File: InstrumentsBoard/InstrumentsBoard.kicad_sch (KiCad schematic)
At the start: 23 parts, among them J1 RJ45_LED_Shielded, Q1 BSS138, U1 Teensy4.1_DEV-16771, U2 OKI

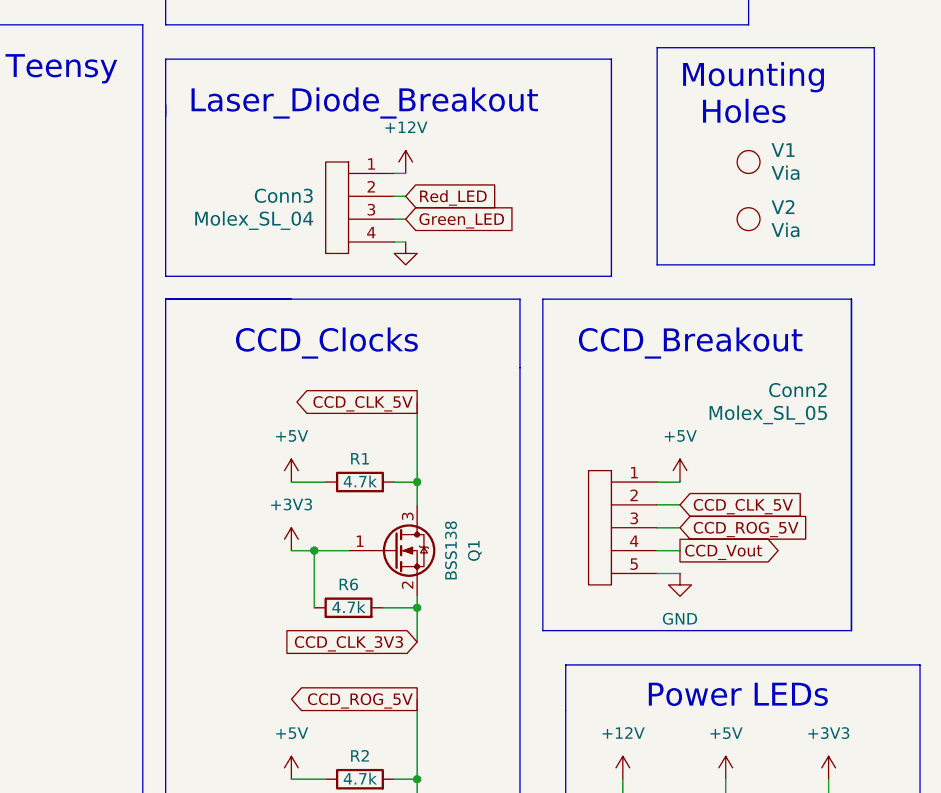
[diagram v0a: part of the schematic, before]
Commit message: change pin ordering for ccd molex
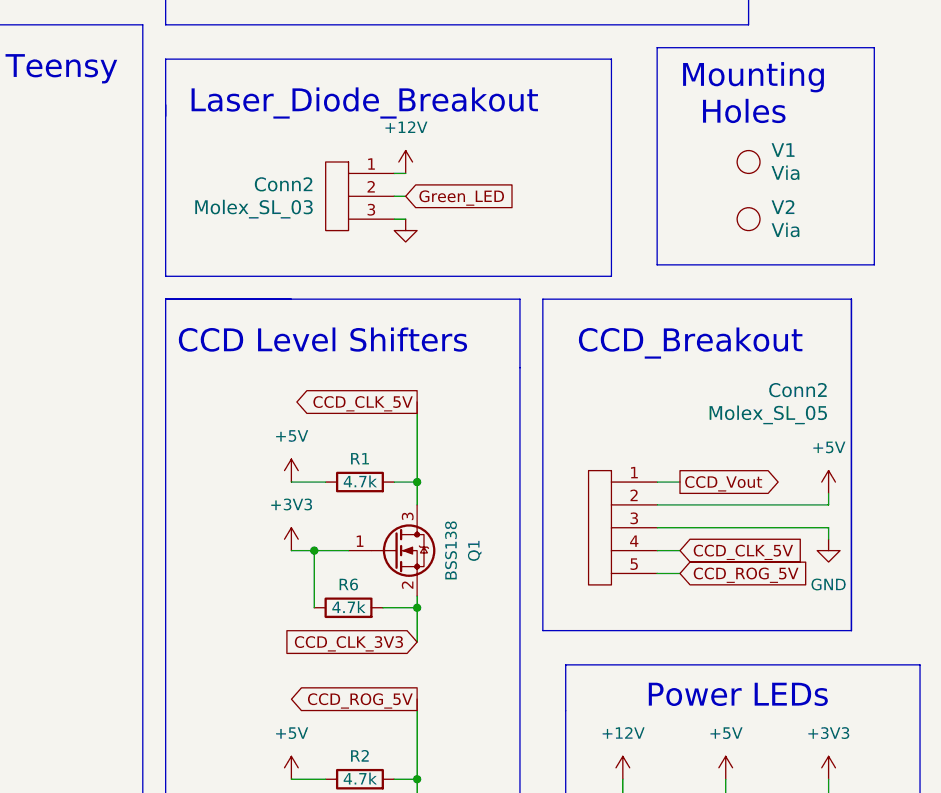
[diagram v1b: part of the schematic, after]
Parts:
- removed Conn3: Molex_SL_04, MRDT_Connectors:MOLEX_SL_04_Vertical, symbol MRDT_Connectors:Molex_SL_04
- added Conn2: Molex_SL_03, MRDT_Connectors:MOLEX_SL_03_Vertical, symbol MRDT_Connectors:Molex_SL_03
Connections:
- net +12V: now also Conn2.1
- net +5V: now also Conn2.2; no longer Conn2.1
- net CCD_CLK_5V: now also Conn2.4; no longer Conn2.2
- net CCD_ROG_5V: now also Conn2.5; no longer Conn2.3
- net CCD_Vout: now also Conn2.1; no longer Conn2.4
- net GND: now also Conn2.3, Conn2.3; no longer Conn2.5
- net Green_LED: now also Conn2.2
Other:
- note added: "CCD Level Shifters"
- note removed: "CCD_Clocks"

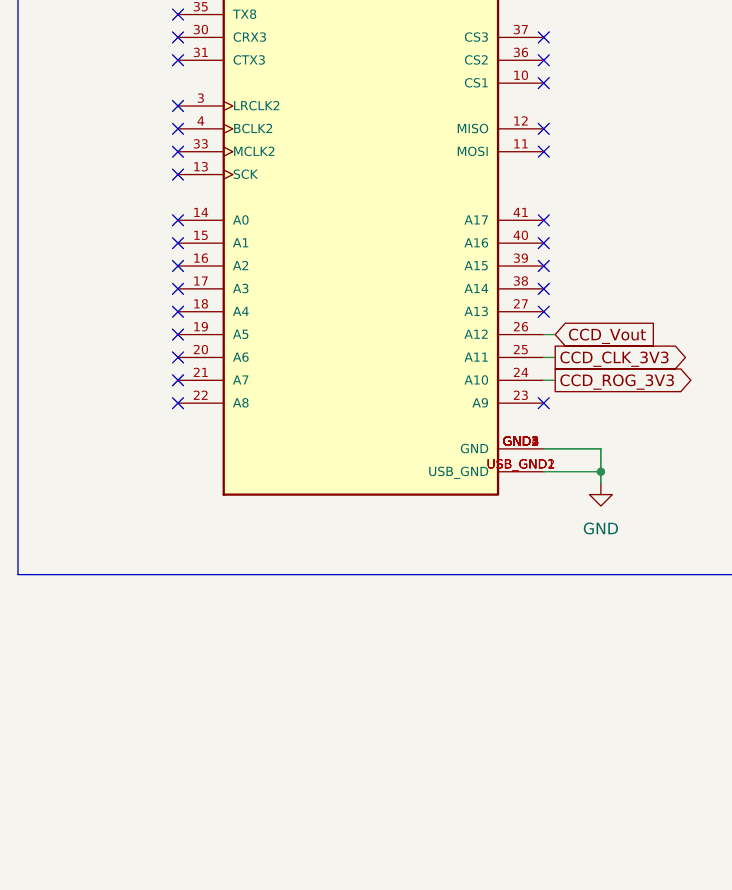
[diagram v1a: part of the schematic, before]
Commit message: Added Hamamatsu Connector, Updated Silkscreen
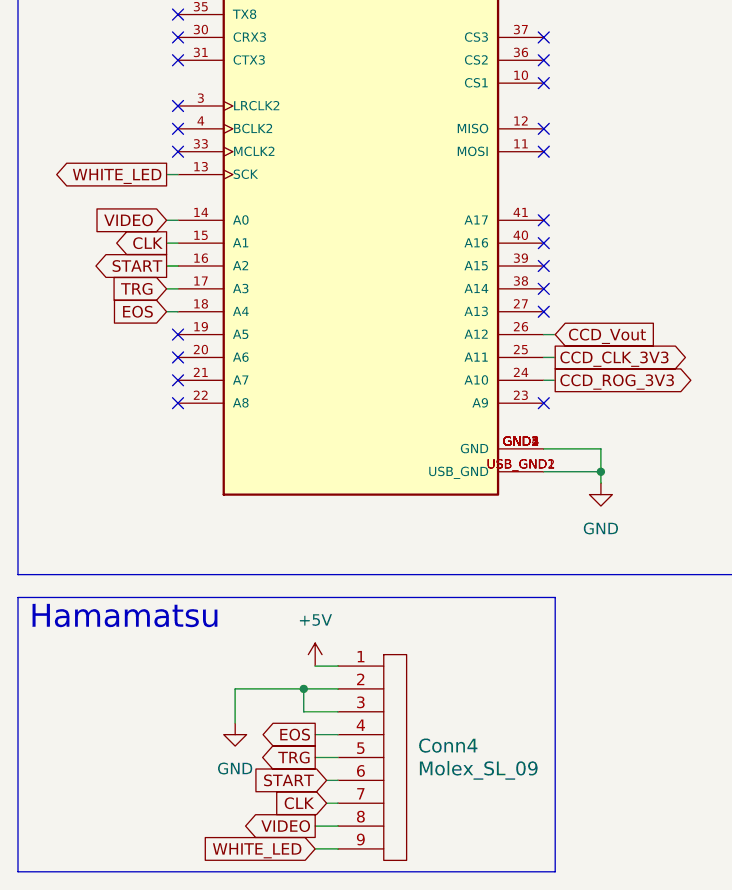
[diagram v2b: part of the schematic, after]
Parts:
- added Conn4: Molex_SL_09, MRDT_Connectors:MOLEX_SL_09_Vertical, symbol MRDT_Connectors:Molex_SL_09
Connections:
- net +5V: now also Conn4.1
- net GND: now also Conn4.2, Conn4.3
- net WHITE_LED: now reaches U1.13 (SCK)
- net WHITE_LED: now also Conn4.9
- net VIDEO: now reaches U1.14 (A0)
- net VIDEO: now also Conn4.8
- net CLK: now reaches U1.15 (A1)
- net CLK: now also Conn4.7
- net START: now reaches U1.16 (A2)
- net START: now also Conn4.6
- net TRG: now reaches U1.17 (A3)
- net TRG: now also Conn4.5
- net EOS: now reaches U1.18 (A4)
- net EOS: now also Conn4.4
- no-connect marks 47 -> 41
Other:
- note added: "Hamamatsu"

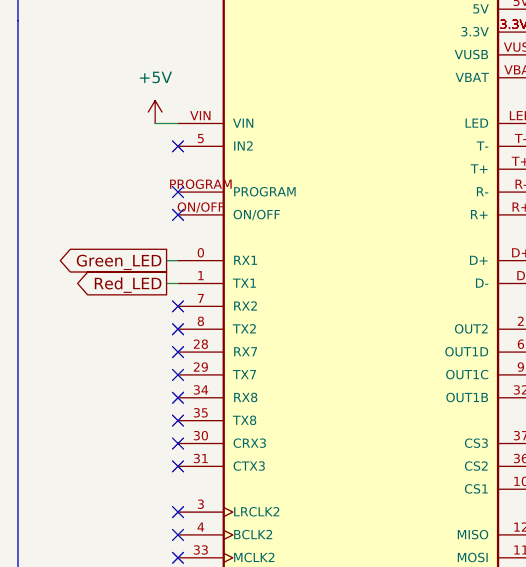
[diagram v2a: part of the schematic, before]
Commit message: Labeled All Pins, Shifted Teensy Over
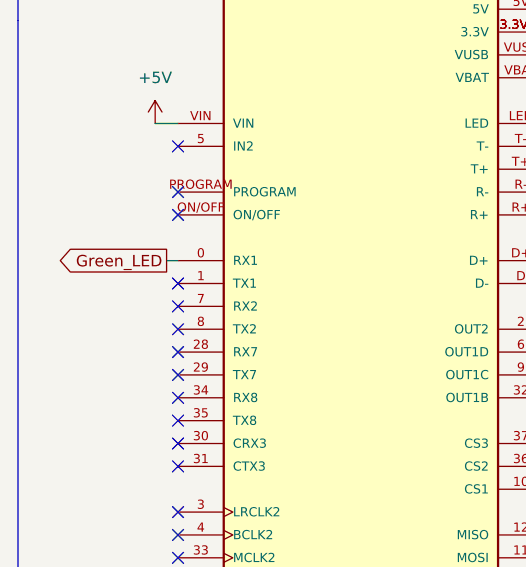
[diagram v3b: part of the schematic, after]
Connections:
- net Red_LED: no longer names the net of U1.1 (TX1)
- no-connect marks 41 -> 42
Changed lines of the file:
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@@
   (no_connect (at 76.2 116.84))
   (no_connect (at 76.2 134.62))
+  (no_connect (at 35.56 104.14))
   (no_connect (at 76.2 114.3))
   (no_connect (at 151.13 43.18))
@@
   )
   (wire (pts (xy 34.29 152.4) (xy 35.56 152.4))
-    (stroke (width 0) (type default))
-  )
-  (wire (pts (xy 34.29 104.14) (xy 35.56 104.14))
     (stroke (width 0) (type default))
   )
@@
       (effects (font (size 1.27 1.27)) (justify right) hide)
     )
-  )
-  (global_label "Red_LED" (shape output) (at 34.29 104.14 180) (fields_autoplaced)
-    (effects (font (size 1.27 1.27)) (justify right))
-    (property "Intersheetrefs" "${INTERSHEET_REFS}" (at 23.3825 104.14 0)
-      (effects (font (size 1.27 1.27)) (justify right) hide)
-    )

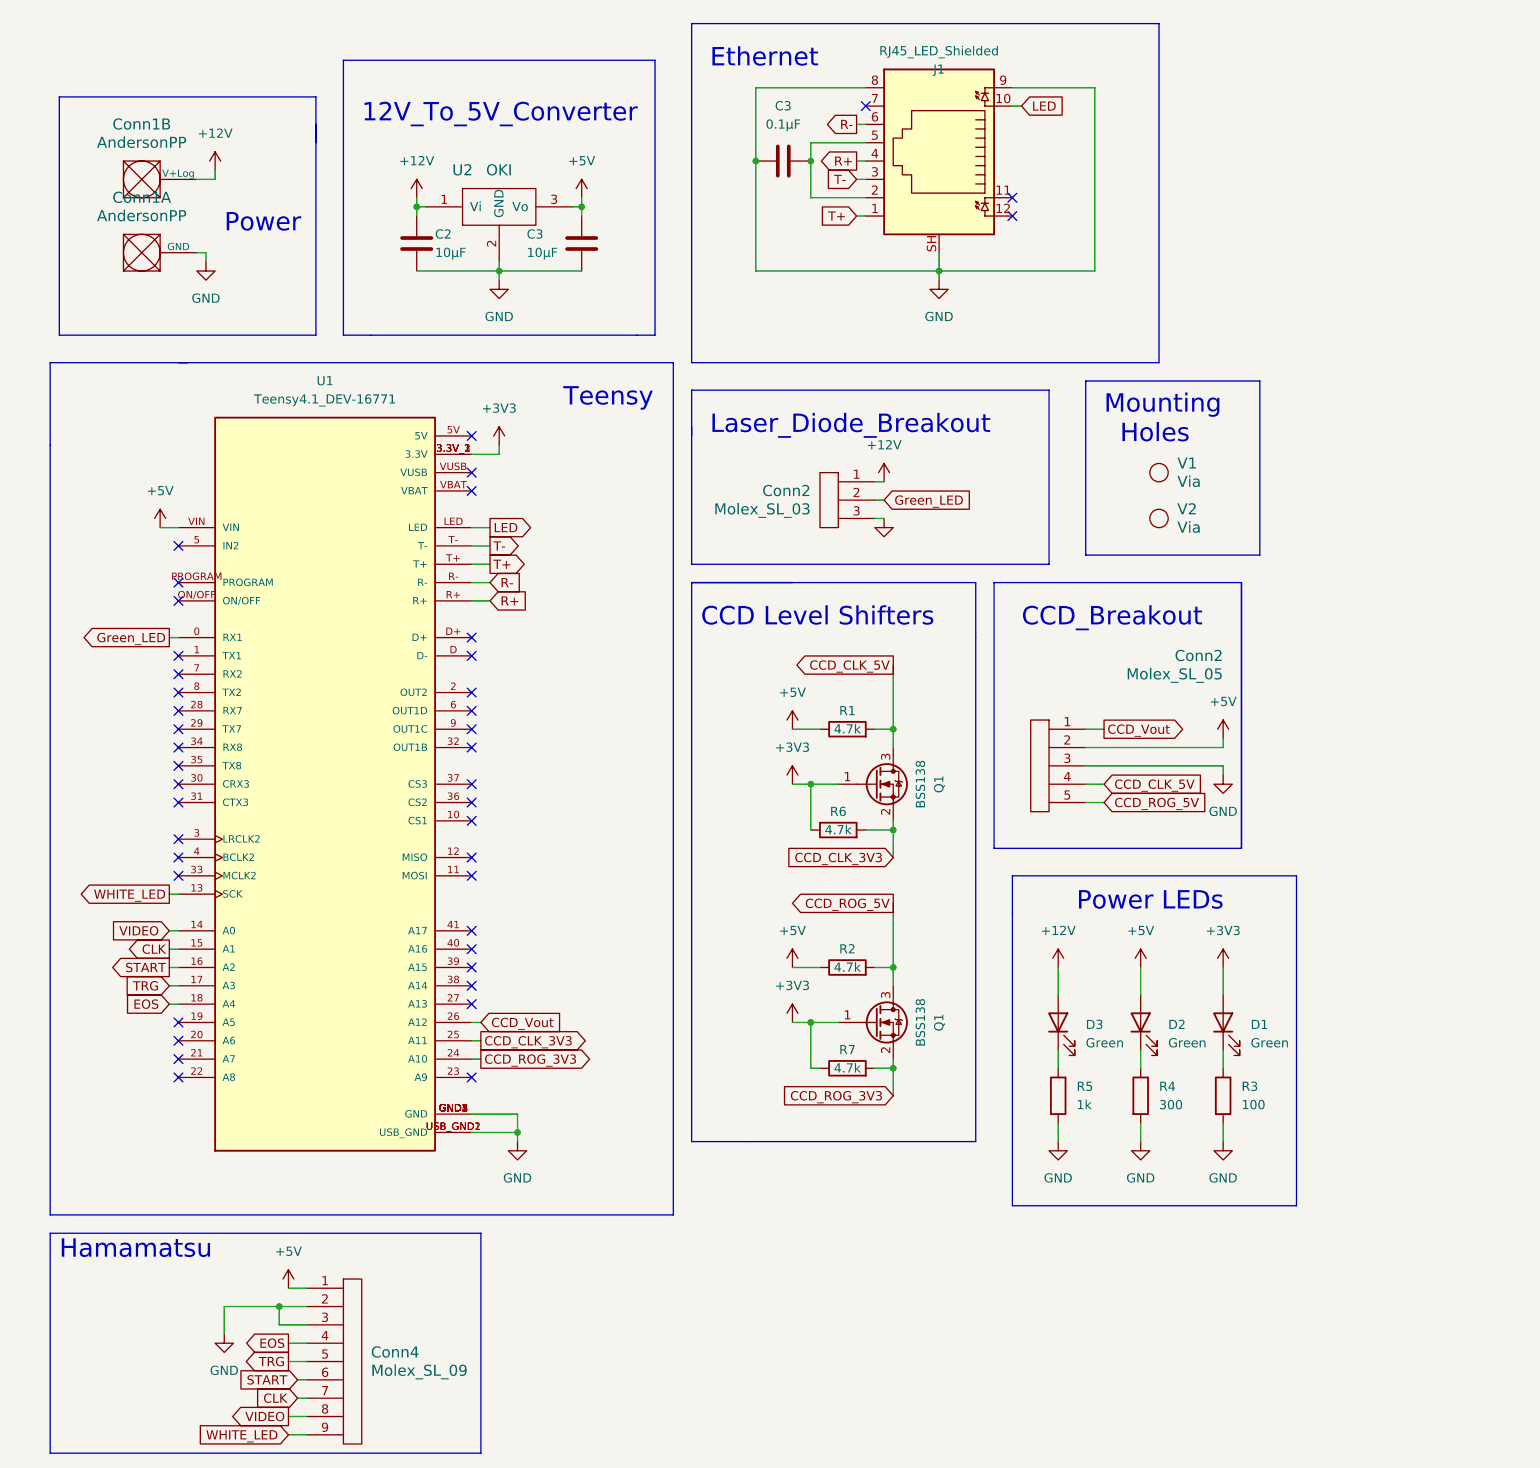
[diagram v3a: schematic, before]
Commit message: remove laser diode board, add laser mosfet
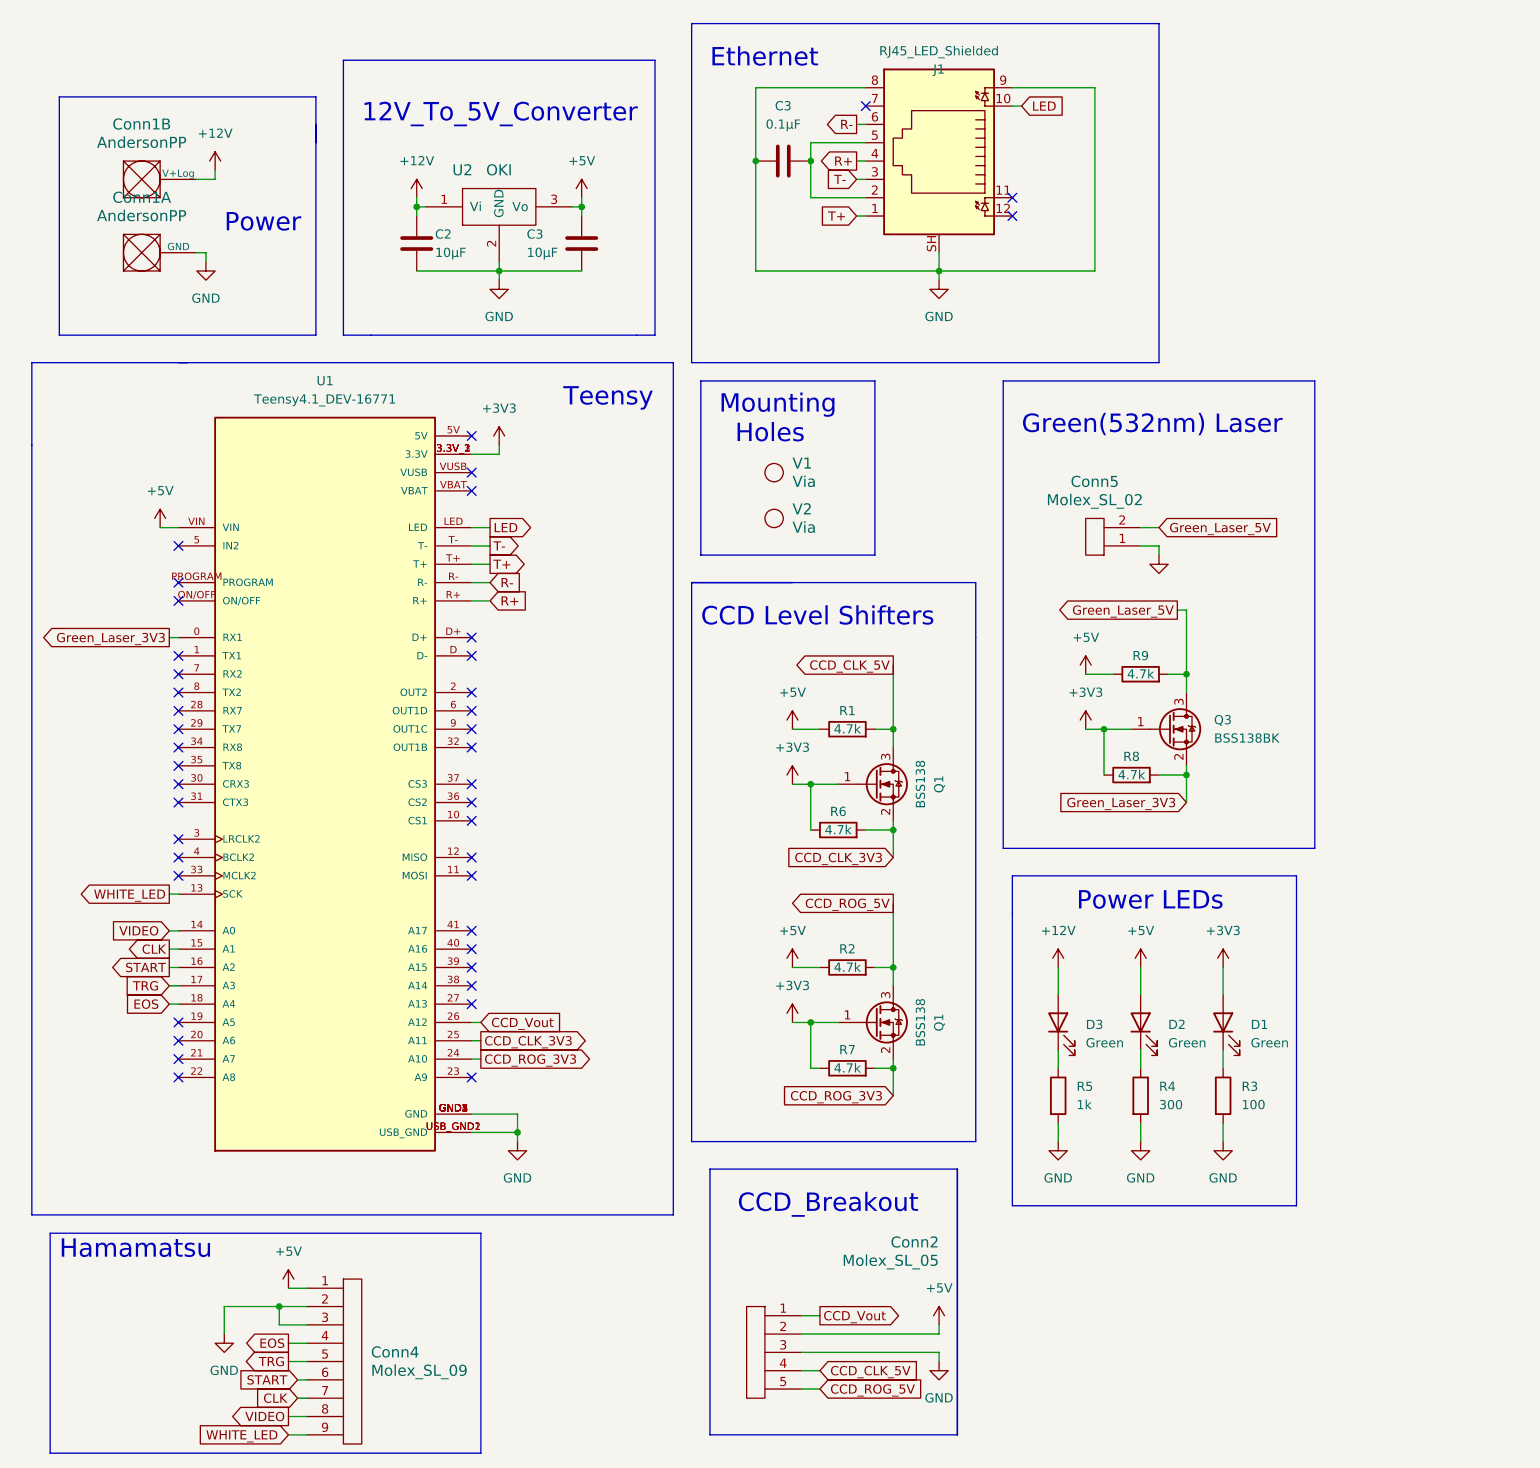
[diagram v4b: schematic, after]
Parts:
- removed Conn2: Molex_SL_03, MRDT_Connectors:MOLEX_SL_03_Vertical, symbol MRDT_Connectors:Molex_SL_03
- added Conn5: Molex_SL_02, MRDT_Connectors:MOLEX_SL_02_Vertical, symbol MRDT_Connectors:Molex_SL_02
- added Q3: BSS138BK, Package_TO_SOT_SMD:SOT-23, symbol Transistor_FET:BSS138
- added R8, R9: 4.7k, Resistor_SMD:R_0603_1608Metric_Pad0.98x0.95mm_HandSolder, symbol Device:R
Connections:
- net +3V3: now also Q3.1 (G), R8.1
- net +5V: now also R9.1
- net GND: now also Conn5.1
- net Green_LED renamed Green_Laser_3V3
- net Green_Laser_3V3: now also Q3.2 (S), R8.2
- new net Green_Laser_5V: Conn5.2, Q3.3 (D), R9.2
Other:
- note added: "Green(532nm) Laser"
- note removed: "Laser_Diode_Breakout"
- moved on the sheet: Conn2, V1, V2

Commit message: board review changes
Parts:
- removed R8, R9: 4.7k, Resistor_SMD:R_0603_1608Metric_Pad0.98x0.95mm_HandSolder, symbol Device:R
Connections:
- net +3V3: no longer Q3.1 (G)
- net +5V: now also Conn5.2
- net GND: now also Q3.2 (S); no longer Conn5.1
- net Green_Laser_3V3: now also Q3.1 (G); no longer Q3.2 (S)
- net Green_Laser_5V: no longer names the net of Q3.3 (D)
- net Green_Laser_5V: now also Conn5.1; no longer Conn5.2
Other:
- moved on the sheet: Conn2, Conn5, D1, D2, D3, Q3, R3, R4, R5
